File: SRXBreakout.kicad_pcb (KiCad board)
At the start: 2 copper layers, 25.4 x 24.1 mm, 19 parts, among them J1 Conn_02x05_Odd_Even, J2 Conn_02x04_Odd_Even

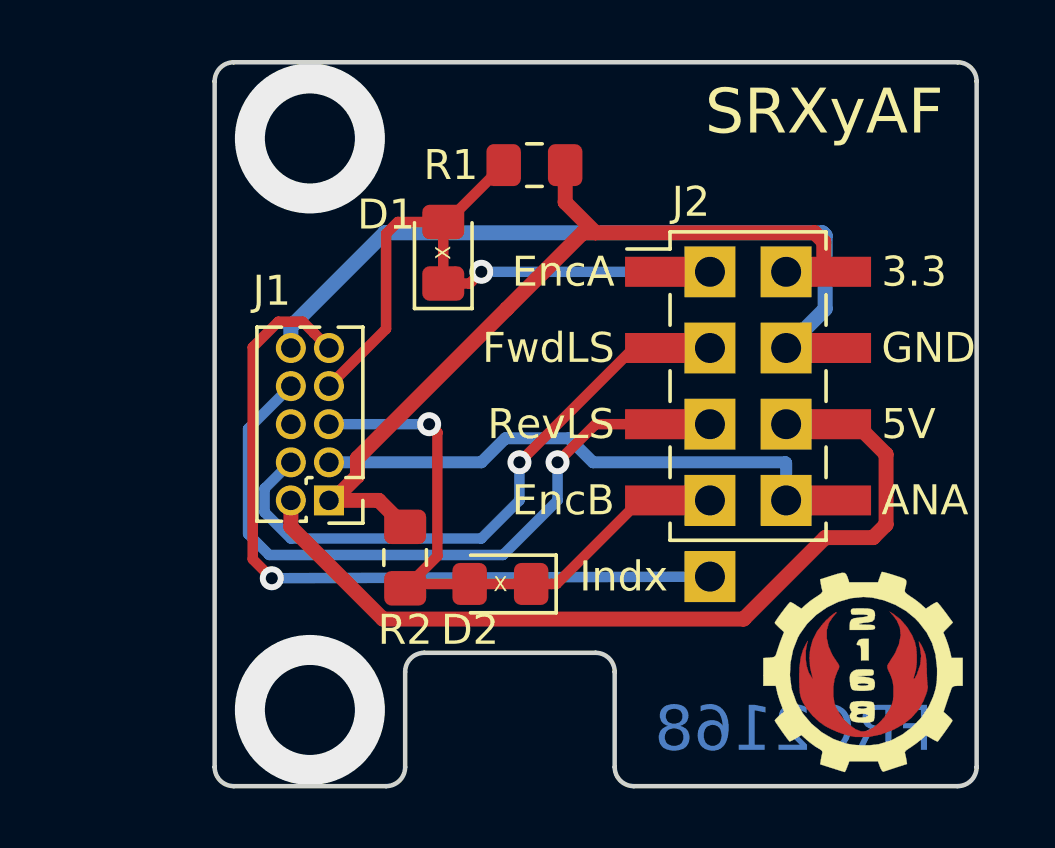
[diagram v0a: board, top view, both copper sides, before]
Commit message: Add status LEDs, switch to 0603 parts, add tab for SPARK Max zip tie
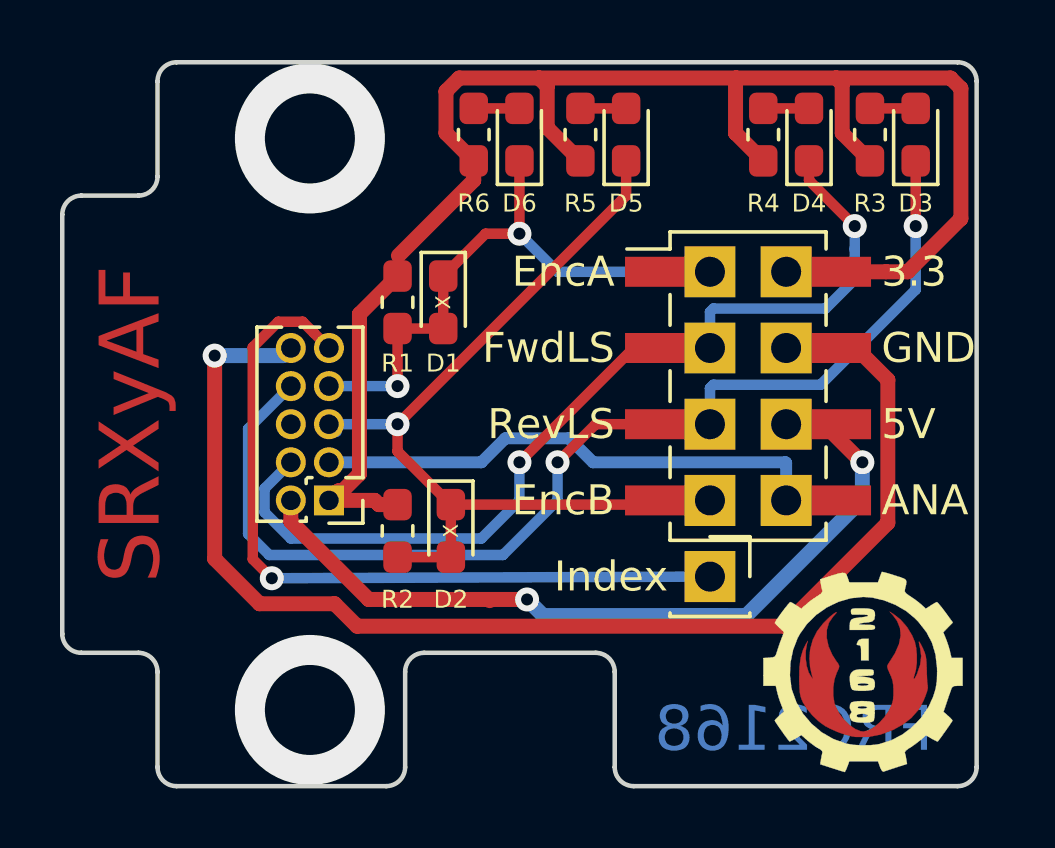
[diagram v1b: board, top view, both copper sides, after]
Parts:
- added D3: LED, Diode_SMD:D_0603_1608Metric_Pad1.05x0.95mm_HandSolder, F.Cu at (175.8, 104.6)
- added D4: LED, Diode_SMD:D_0603_1608Metric_Pad1.05x0.95mm_HandSolder, F.Cu at (172.2, 104.6)
- added D5: LED, Diode_SMD:D_0603_1608Metric_Pad1.05x0.95mm_HandSolder, F.Cu at (166.1, 104.6)
- added D6: LED, Diode_SMD:D_0603_1608Metric_Pad1.05x0.95mm_HandSolder, F.Cu at (162.6, 104.6)
- added R3: 390, Resistor_SMD:R_0603_1608Metric_Pad1.05x0.95mm_HandSolder, F.Cu at (174.2, 104.6)
- added R4: 390, Resistor_SMD:R_0603_1608Metric_Pad1.05x0.95mm_HandSolder, F.Cu at (170.7, 104.6)
- added R5: 390, Resistor_SMD:R_0603_1608Metric_Pad1.05x0.95mm_HandSolder, F.Cu at (164.6, 104.6)
- added R6: 390, Resistor_SMD:R_0603_1608Metric_Pad1.05x0.95mm_HandSolder, F.Cu at (161.0, 104.6)
- D1, D2: footprint Diode_SMD:D_0805_2012Metric_Pad1.15x1.40mm_HandSolder -> Diode_SMD:D_0603_1608Metric_Pad1.05x0.95mm_HandSolder
- R1, R2: footprint Resistor_SMD:R_0805_2012Metric_Pad1.15x1.40mm_HandSolder -> Resistor_SMD:R_0603_1608Metric_Pad1.05x0.95mm_HandSolder
- TP1, TP2, TP3, TP4, TP5, TP6, TP7, TP8, TP9: footprint footprint_mods:PinSocket_1x01_P2.54mm_Vertical -> Connector_PinSocket_2.54mm:PinSocket_1x01_P2.54mm_Vertical
- moved R1 6.46 mm to (158.5, 110.2), turned to 270 degrees
- moved D2 2.42 mm to (160.3, 117.9), turned to 270 degrees
- moved D1 1.65 mm to (160.0, 110.2), turned to 270 degrees
- moved R2 0.92 mm to (158.5, 117.9)
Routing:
- net 3.3V: track 28.3 -> 55.8 mm
- net GND: track 24.8 -> 42.4 mm, vias 0 -> 1
- net RevLim: track 23.8 -> 37.5 mm, vias 1 -> 2
- net FwdLim: track 20.4 -> 31.5 mm, vias 1 -> 2
- net QuadratureB: track 19.7 -> 30.0 mm
- net QuadratureA: track 22.4 -> 19.9 mm, vias 1 -> 2
- net Net-(D6-Pad2): track 0.00 -> 1.52 mm
- net Net-(D5-Pad2): track 0.00 -> 1.52 mm
- net Net-(D4-Pad2): track 0.00 -> 1.52 mm
- net Net-(D3-Pad2): track 0.00 -> 1.52 mm
- net 5V: track 28.1 -> 28.5 mm, vias 0 -> 2
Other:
- board size 25.4 x 24.1 mm -> 30.5 x 24.1 mm
- board text added: "200113.01"
- board text added: "Index"
- board text removed: "190122.01"
- board text removed: "Indx"
